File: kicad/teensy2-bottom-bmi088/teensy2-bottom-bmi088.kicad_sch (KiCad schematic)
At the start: 11 parts, among them J1 Conn_01x14_Socket, J2 Conn_01x14_Socket, J3 Conn_01x03_Socket, J4 Conn_01x03_Socket, J5 Conn_01x06_Pin, J6 Conn_01x02_Socket, J7 Conn_01x08_Pin

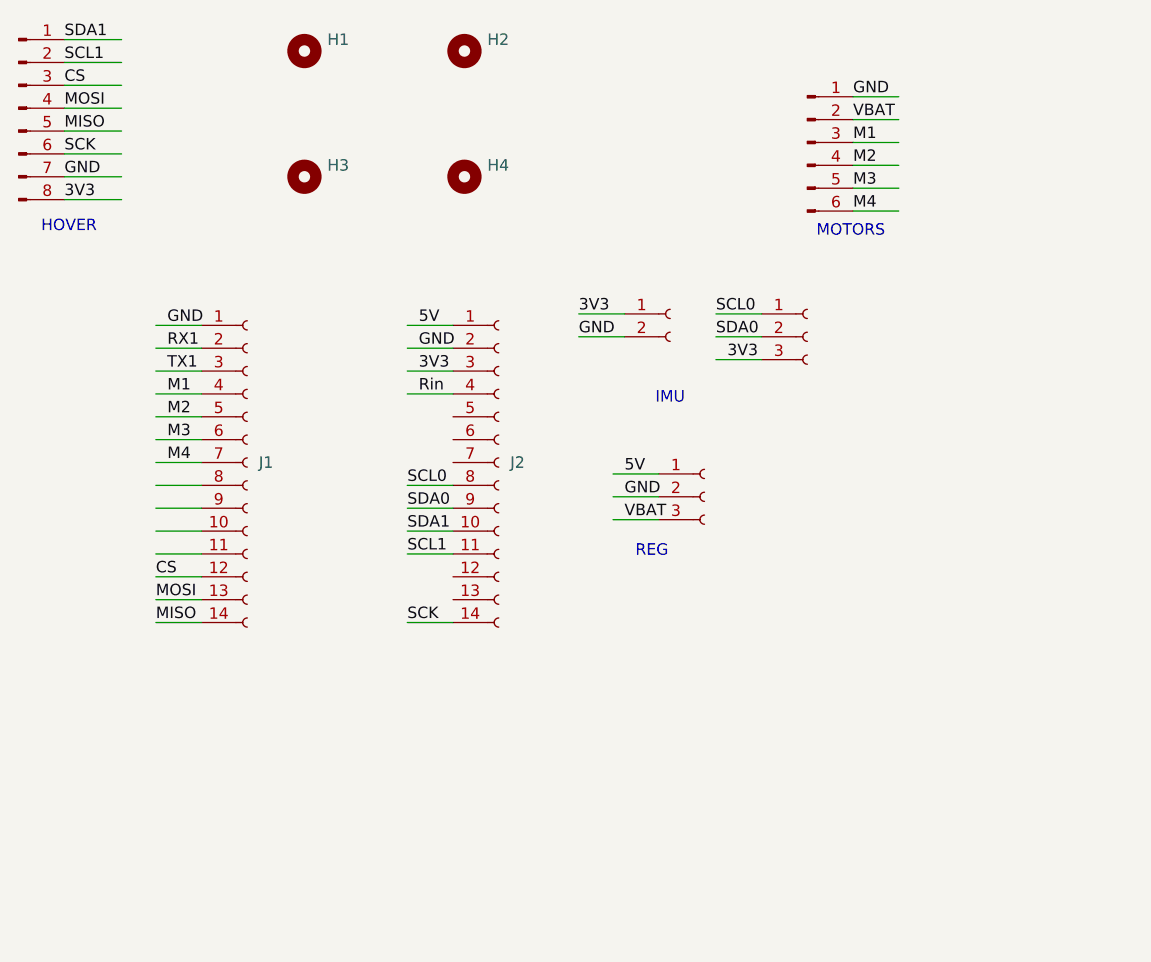
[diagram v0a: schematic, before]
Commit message: modified:   kicad/teensy2-bottom-bmi088/teensy2-bottom-bmi088.kicad_pcb
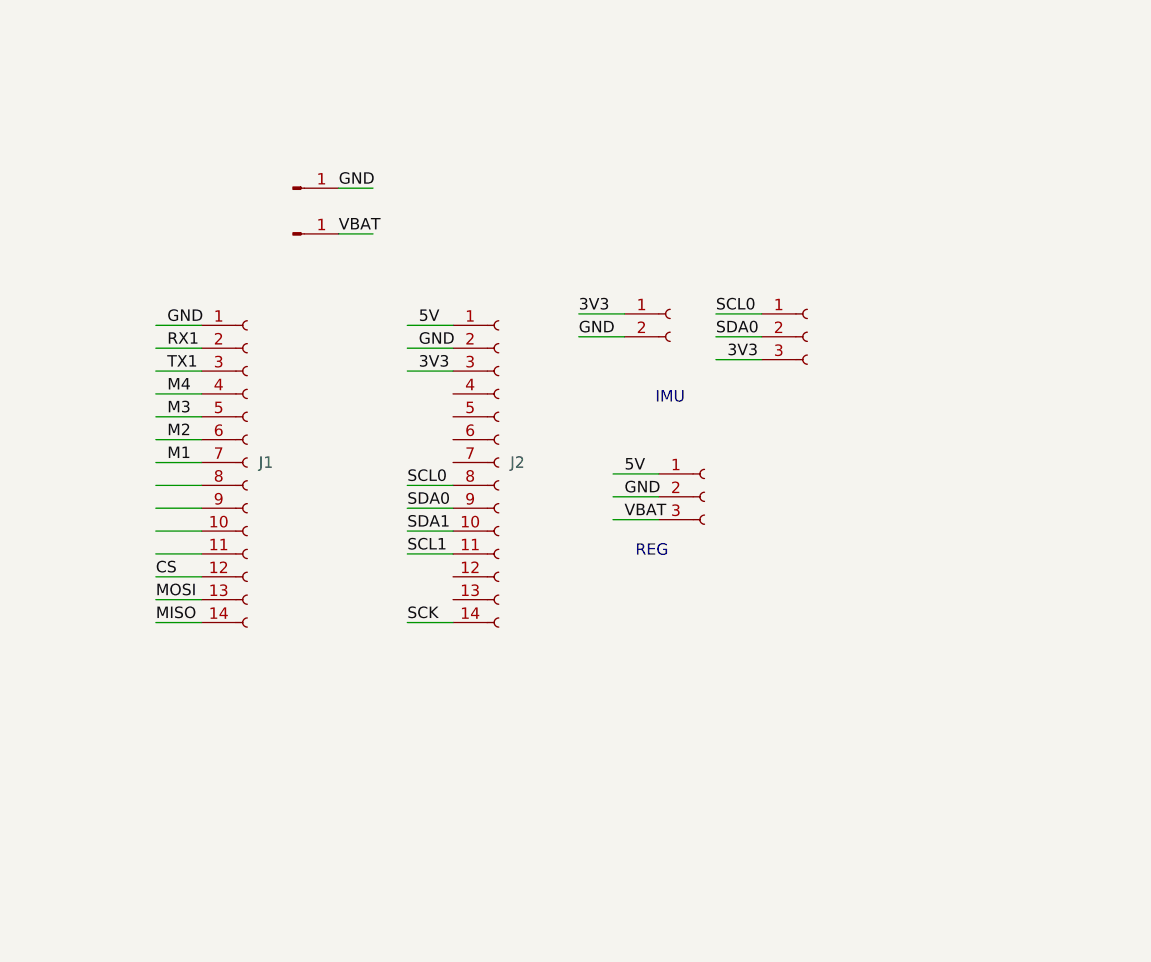
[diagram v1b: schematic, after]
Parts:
- removed H1, H2, H3, H4: MountingHole, MountingHole:MountingHole_2.5mm, symbol Mechanical:MountingHole
- removed J5: Conn_01x06_Pin, Connector_PinHeader_2.00mm:PinHeader_1x06_P2.00mm_Vertical, symbol Connector:Conn_01x06_Pin
- removed J7: Conn_01x08_Pin, Connector_PinSocket_2.00mm:PinSocket_1x08_P2.00mm_Vertical, symbol Connector:Conn_01x08_Pin
- added J5, J7: Conn_01x01_Pin, Connector_Wire:SolderWirePad_1x01_SMD_1x2mm, symbol Connector:Conn_01x01_Pin
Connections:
- net GND: now also J5.1 (Pin_1)
- net M1: now also J1.7 (Pin_7); no longer J1.4 (Pin_4)
- net M2: now also J1.6 (Pin_6); no longer J1.5 (Pin_5)
- net M3: now also J1.5 (Pin_5); no longer J1.6 (Pin_6)
- net M4: now also J1.4 (Pin_4); no longer J1.7 (Pin_7)
- net VBAT: now also J7.1 (Pin_1)
- net Rin: no longer names the net of J2.4 (Pin_4)
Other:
- note removed: "HOVER"
- note removed: "MOTORS"

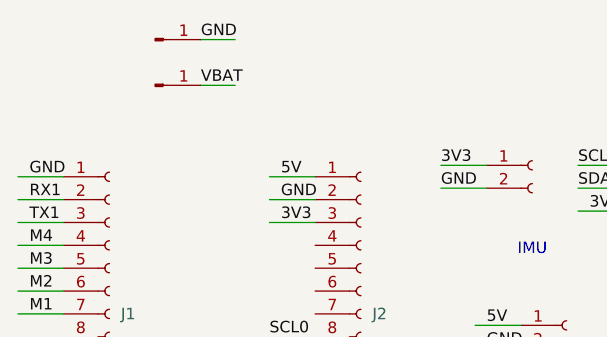
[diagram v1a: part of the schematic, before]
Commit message: modified:   kicad/teensy2-bottom-bmi088/teensy2-bottom-bmi088.kicad_pcb
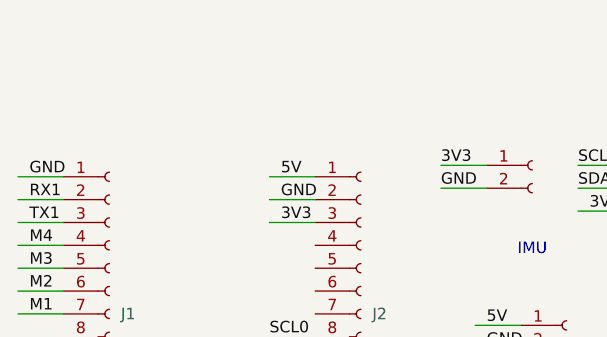
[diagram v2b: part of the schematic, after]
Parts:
- removed J5, J7: Conn_01x01_Pin, Connector_Wire:SolderWirePad_1x01_SMD_1x2mm, symbol Connector:Conn_01x01_Pin
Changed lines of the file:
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@@
-	(wire
-		(pts
-			(xy 111.76 88.9) (xy 115.57 88.9)
-		)
-		(stroke
-			(width 0)
-			(type default)
-		)
-	)
 	(wire
 		(pts
@@
 		(pts
 			(xy 142.24 115.57) (xy 147.32 115.57)
-		)
-		(stroke
-			(width 0)
-			(type default)
-		)
-	)
-	(wire
-		(pts
-			(xy 111.76 83.82) (xy 115.57 83.82)
 		)
 		(stroke
@@
 		)
 	)
-	(label "VBAT"
-		(at 111.76 88.9 0)
-		(effects
-			(font
-				(size 1.27 1.27)
-			)
-			(justify left bottom)
-		)
-	)
 	(label "GND"
 		(at 143.51 118.11 0)
@@
 	(label "TX1"
 		(at 92.71 104.14 0)
-		(effects
-			(font
-				(size 1.27 1.27)
-			)
-			(justify left bottom)
-		)
-	)
-	(label "GND"
-		(at 111.76 83.82 0)
 		(effects
 			(font
@@
 					(unit 1)
 				)
-			)
-		)
-	)
-	(symbol
-		(lib_id "Connector:Conn_01x01_Pin")
-		(at 106.68 83.82 0)
-		(unit 1)
-		(exclude_from_sim no)
-		(in_bom yes)
-		(on_board yes)
-		(dnp no)
-		(fields_autoplaced yes)
-		(property "Reference" "J5"
-			(at 107.315 78.74 0)
-			(effects
-				(font
-					(size 1.27 1.27)
-				)
-				(hide yes)
-			)
-		)
-		(property "Value" "Conn_01x01_Pin"
-			(at 107.315 81.28 0)
-			(effects
-				(font
-					(size 1.27 1.27)
-				)
-				(hide yes)
-			)
-		)
-		(property "Footprint" "Connector_Wire:SolderWirePad_1x01_SMD_1x2mm"
-			(at 106.68 83.82 0)
-			(effects
-				(font
-					(size 1.27 1.27)
-				)
-				(hide yes)
-			)
-		)
-		(property "Datasheet" "~"
-			(at 106.68 83.82 0)
-			(effects
-				(font
-					(size 1.27 1.27)
-				)
-				(hide yes)
-			)
-		)
-		(property "Description" "Generic connector, single row, 01x01, script generated"
-			(at 106.68 83.82 0)
-			(effects
-				(font
-					(size 1.27 1.27)
-				)
-				(hide yes)
-			)
-		)
-		(pin "1"
-		)
-		(instances
-			(project ""
-				(path "/2b1f0318-b347-4cb8-9bbf-78e69ec66761"
-					(reference "J5")
-					(unit 1)
-				)
-			)
-		)
-	)
-	(symbol
-		(lib_id "Connector:Conn_01x01_Pin")
-		(at 106.68 88.9 0)
-		(unit 1)
-		(exclude_from_sim no)
-		(in_bom yes)
-		(on_board yes)
-		(dnp no)
-		(fields_autoplaced yes)
-		(property "Reference" "J7"
-			(at 107.315 83.82 0)
-			(effects
-				(font
-					(size 1.27 1.27)
-				)
-				(hide yes)
-			)
-		)
-		(property "Value" "Conn_01x01_Pin"
-			(at 107.315 86.36 0)
-			(effects
-				(font
-					(size 1.27 1.27)
-				)
-				(hide yes)
-			)
-		)
-		(property "Footprint" "Connector_Wire:SolderWirePad_1x01_SMD_1x2mm"
-			(at 106.68 88.9 0)
-			(effects
-				(font
-					(size 1.27 1.27)
-				)
-				(hide yes)
-			)
-		)
-		(property "Datasheet" "~"
-			(at 106.68 88.9 0)
-			(effects
-				(font
-					(size 1.27 1.27)
-				)
-				(hide yes)
-			)
-		)
-		(property "Description" "Generic connector, single row, 01x01, script generated"
-			(at 106.68 88.9 0)
-			(effects
-				(font
-					(size 1.27 1.27)
-				)
-				(hide yes)
-			)
-		)
-		(pin "1"
-		)
-		(instances
-			(project "teensy2-bottom-bmi088"
-				(path "/2b1f0318-b347-4cb8-9bbf-78e69ec66761"
-					(reference "J7")
-					(unit 1)
-				)

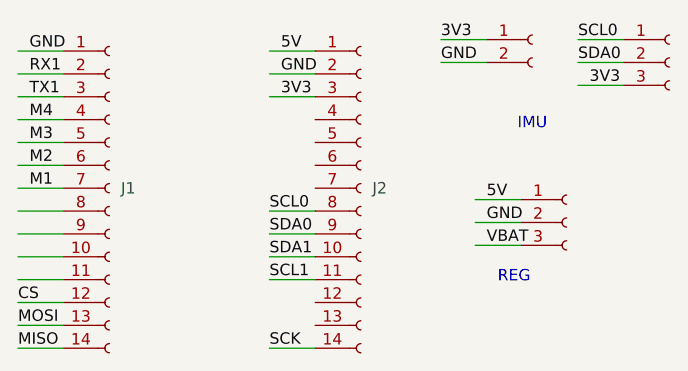
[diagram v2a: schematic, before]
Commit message: modified:   kicad/teensy2-bottom-bmi088/teensy2-bottom-bmi088.kicad_pcb
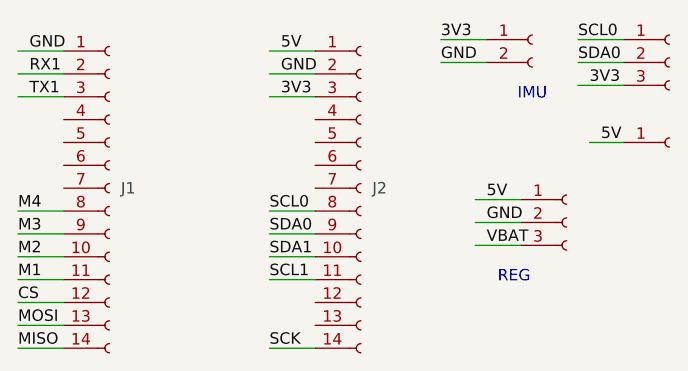
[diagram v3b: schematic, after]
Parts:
- added J5: Conn_01x01_Socket, Connector_Wire:SolderWirePad_1x01_SMD_1x2mm, symbol Connector:Conn_01x01_Socket
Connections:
- net 5V: now also J5.1 (Pin_1)
- net M1: now also J1.11 (Pin_11); no longer J1.7 (Pin_7)
- net M2: now also J1.10 (Pin_10); no longer J1.6 (Pin_6)
- net M3: now also J1.9 (Pin_9); no longer J1.5 (Pin_5)
- net M4: now also J1.8 (Pin_8); no longer J1.4 (Pin_4)
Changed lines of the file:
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@@
 	(text "IMU"
 		(exclude_from_sim no)
-		(at 148.59 107.188 0)
+		(at 148.59 103.886 0)
 		(effects
 			(font
@@
 	(wire
 		(pts
-			(xy 91.44 111.76) (xy 96.52 111.76)
-		)
-		(stroke
-			(width 0)
-			(type default)
-		)
-	)
-	(wire
-		(pts
 			(xy 91.44 101.6) (xy 96.52 101.6)
 		)
@@
 	(wire
 		(pts
-			(xy 91.44 106.68) (xy 96.52 106.68)
-		)
-		(stroke
-			(width 0)
-			(type default)
-		)
-	)
-	(wire
-		(pts
 			(xy 153.67 100.33) (xy 158.75 100.33)
 		)
@@
 	(wire
 		(pts
-			(xy 91.44 114.3) (xy 96.52 114.3)
-		)
-		(stroke
-			(width 0)
-			(type default)
-		)
-	)
-	(wire
-		(pts
 			(xy 91.44 116.84) (xy 96.52 116.84)
 		)
@@
 	(wire
 		(pts
-			(xy 91.44 109.22) (xy 96.52 109.22)
-		)
-		(stroke
-			(width 0)
-			(type default)
-		)
-	)
-	(wire
-		(pts
 			(xy 91.44 124.46) (xy 96.52 124.46)
 		)
@@
 		(pts
 			(xy 119.38 104.14) (xy 124.46 104.14)
+		)
+		(stroke
+			(width 0)
+			(type default)
+		)
+	)
+	(wire
+		(pts
+			(xy 154.94 109.22) (xy 158.75 109.22)
 		)
 		(stroke
@@
 		)
 	)
+	(label "M1"
+		(at 91.44 124.46 0)
+		(effects
+			(font
+				(size 1.27 1.27)
+			)
+			(justify left bottom)
+		)
+	)
 	(label "GND"
 		(at 92.71 99.06 0)
@@
 		)
 	)
+	(label "M2"
+		(at 91.44 121.92 0)
+		(effects
+			(font
+				(size 1.27 1.27)
+			)
+			(justify left bottom)
+		)
+	)
 	(label "MISO"
 		(at 91.44 132.08 0)
@@
 		)
 	)
+	(label "M4"
+		(at 91.44 116.84 0)
+		(effects
+			(font
+				(size 1.27 1.27)
+			)
+			(justify left bottom)
+		)
+	)
 	(label "SCL0"
 		(at 119.38 116.84 0)
@@
 		)
 	)
+	(label "M3"
+		(at 91.44 119.38 0)
+		(effects
+			(font
+				(size 1.27 1.27)
+			)
+			(justify left bottom)
+		)
+	)
 	(label "GND"
 		(at 143.51 118.11 0)
@@
 		)
 	)
-	(label "M1"
-		(at 92.71 114.3 0)
-		(effects
-			(font
-				(size 1.27 1.27)
-			)
-			(justify left bottom)
-		)
-	)
-	(label "M3"
-		(at 92.71 109.22 0)
-		(effects
-			(font
-				(size 1.27 1.27)
-			)
-			(justify left bottom)
-		)
-	)
-	(label "M2"
-		(at 92.71 111.76 0)
-		(effects
-			(font
-				(size 1.27 1.27)
-			)
-			(justify left bottom)
-		)
-	)
 	(label "3V3"
 		(at 138.43 97.79 0)
@@
 		)
 	)
-	(label "M4"
-		(at 92.71 106.68 0)
-		(effects
-			(font
-				(size 1.27 1.27)
-			)
-			(justify left bottom)
-		)
-	)
 	(label "TX1"
 		(at 92.71 104.14 0)
@@
 	(label "RX1"
 		(at 92.71 101.6 0)
+		(effects
+			(font
+				(size 1.27 1.27)
+			)
+			(justify left bottom)
+		)
+	)
+	(label "5V"
+		(at 156.21 109.22 0)
 		(effects
 			(font
@@
 					(unit 1)
 				)
+			)
+		)
+	)
+	(symbol
+		(lib_id "Connector:Conn_01x01_Socket")
+		(at 163.83 109.22 0)
+		(unit 1)
+		(exclude_from_sim no)
+		(in_bom yes)
+		(on_board yes)
+		(dnp no)
+		(fields_autoplaced yes)
+		(property "Reference" "J5"
+			(at 165.1 107.9499 0)
+			(effects
+				(font
+					(size 1.27 1.27)
+				)
+				(justify left)
+				(hide yes)
+			)
+		)
+		(property "Value" "Conn_01x01_Socket"
+			(at 165.1 110.4899 0)
+			(effects
+				(font
+					(size 1.27 1.27)
+				)
+				(justify left)
+				(hide yes)
+			)
+		)
+		(property "Footprint" "Connector_Wire:SolderWirePad_1x01_SMD_1x2mm"
+			(at 163.83 109.22 0)
+			(effects
+				(font
+					(size 1.27 1.27)
+				)
+				(hide yes)
+			)
+		)
+		(property "Datasheet" "~"
+			(at 163.83 109.22 0)
+			(effects
+				(font
+					(size 1.27 1.27)
+				)
+				(hide yes)
+			)
+		)
+		(property "Description" "Generic connector, single row, 01x01, script generated"
+			(at 163.83 109.22 0)
+			(effects
+				(font
+					(size 1.27 1.27)
+				)
+				(hide yes)
+			)
+		)
+		(pin "1"
+		)
+		(instances
+			(project ""
+				(path "/2b1f0318-b347-4cb8-9bbf-78e69ec66761"
+					(reference "J5")
+					(unit 1)
+				)

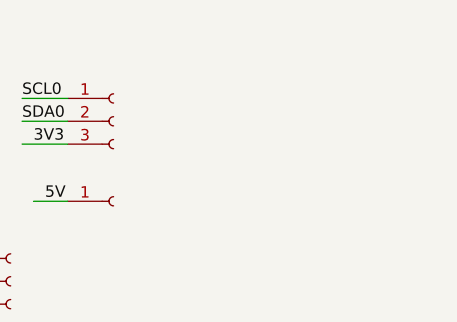
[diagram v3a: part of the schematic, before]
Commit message: modified:   kicad/teensy2-bottom-bmi088/teensy2-bottom-bmi088.kicad_pcb
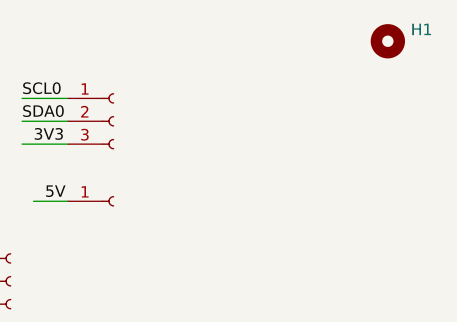
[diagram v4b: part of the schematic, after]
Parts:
- added H1: MountingHole, MountingHole:MountingHole_2.5mm, symbol Mechanical:MountingHole
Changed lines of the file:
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@@
+	)
+	(symbol
+		(lib_id "Mechanical:MountingHole")
+		(at 194.31 91.44 0)
+		(unit 1)
+		(exclude_from_sim no)
+		(in_bom no)
+		(on_board yes)
+		(dnp no)
+		(fields_autoplaced yes)
+		(property "Reference" "H1"
+			(at 196.85 90.1699 0)
+			(effects
+				(font
+					(size 1.27 1.27)
+				)
+				(justify left)
+			)
+		)
+		(property "Value" "MountingHole"
+			(at 196.85 92.7099 0)
+			(effects
+				(font
+					(size 1.27 1.27)
+				)
+				(justify left)
+				(hide yes)
+			)
+		)
+		(property "Footprint" "MountingHole:MountingHole_2.5mm"
+			(at 194.31 91.44 0)
+			(effects
+				(font
+					(size 1.27 1.27)
+				)
+				(hide yes)
+			)
+		)
+		(property "Datasheet" "~"
+			(at 194.31 91.44 0)
+			(effects
+				(font
+					(size 1.27 1.27)
+				)
+				(hide yes)
+			)
+		)
+		(property "Description" "Mounting Hole without connection"
+			(at 194.31 91.44 0)
+			(effects
+				(font
+					(size 1.27 1.27)
+				)
+				(hide yes)
+			)
+		)
+		(instances
+			(project "teensy2-bottom-bmi088"
+				(path "/2b1f0318-b347-4cb8-9bbf-78e69ec66761"
+					(reference "H1")
+					(unit 1)
+				)
+			)
+		)
 	)
 	(symbol

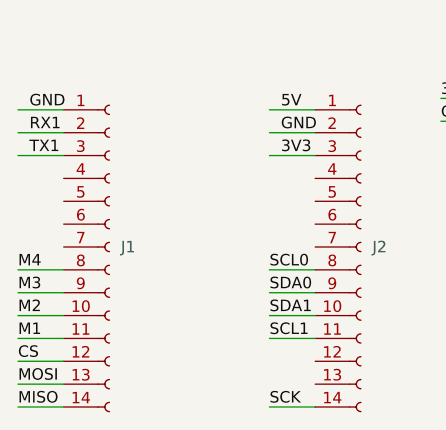
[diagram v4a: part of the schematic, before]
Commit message: modified:   kicad/teensy2-bottom-bmi088/teensy2-bottom-bmi088.kicad_pcb
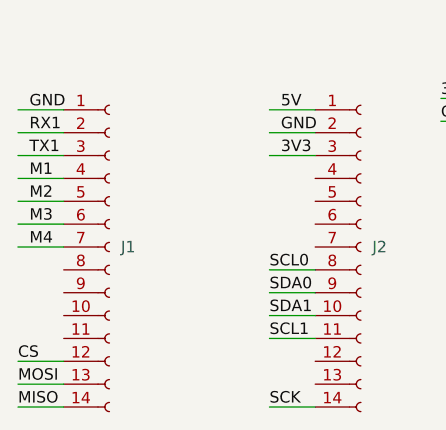
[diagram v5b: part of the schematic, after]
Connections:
- net M1: now also J1.4 (Pin_4); no longer J1.11 (Pin_11)
- net M2: now also J1.5 (Pin_5); no longer J1.10 (Pin_10)
- net M3: now also J1.6 (Pin_6); no longer J1.9 (Pin_9)
- net M4: now also J1.7 (Pin_7); no longer J1.8 (Pin_8)
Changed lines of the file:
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@@
+	(wire
+		(pts
+			(xy 91.44 114.3) (xy 96.52 114.3)
+		)
+		(stroke
+			(width 0)
+			(type default)
+		)
+	)
 	(wire
 		(pts
@@
 	(wire
 		(pts
+			(xy 91.44 111.76) (xy 96.52 111.76)
+		)
+		(stroke
+			(width 0)
+			(type default)
+		)
+	)
+	(wire
+		(pts
 			(xy 119.38 119.38) (xy 124.46 119.38)
 		)
@@
 	(wire
 		(pts
-			(xy 91.44 121.92) (xy 96.52 121.92)
-		)
-		(stroke
-			(width 0)
-			(type default)
-		)
-	)
-	(wire
-		(pts
 			(xy 153.67 100.33) (xy 158.75 100.33)
 		)
@@
 	(wire
 		(pts
-			(xy 91.44 116.84) (xy 96.52 116.84)
+			(xy 91.44 106.68) (xy 96.52 106.68)
 		)
 		(stroke
@@
 	(wire
 		(pts
+			(xy 91.44 109.22) (xy 96.52 109.22)
+		)
+		(stroke
+			(width 0)
+			(type default)
+		)
+	)
+	(wire
+		(pts
 			(xy 153.67 97.79) (xy 158.75 97.79)
 		)
@@
 		(pts
 			(xy 91.44 104.14) (xy 96.52 104.14)
-		)
-		(stroke
-			(width 0)
-			(type default)
-		)
-	)
-	(wire
-		(pts
-			(xy 91.44 124.46) (xy 96.52 124.46)
-		)
-		(stroke
-			(width 0)
-			(type default)
-		)
-	)
-	(wire
-		(pts
-			(xy 91.44 119.38) (xy 96.52 119.38)
 		)
 		(stroke
@@
 		)
 	)
-	(label "M1"
-		(at 91.44 124.46 0)
+	(label "M2"
+		(at 92.71 109.22 0)
 		(effects
 			(font
@@
 		)
 	)
-	(label "M2"
-		(at 91.44 121.92 0)
-		(effects
-			(font
-				(size 1.27 1.27)
-			)
-			(justify left bottom)
-		)
-	)
 	(label "MISO"
 		(at 91.44 132.08 0)
@@
 		)
 	)
-	(label "M4"
-		(at 91.44 116.84 0)
+	(label "M3"
+		(at 92.71 111.76 0)
 		(effects
 			(font
@@
 		)
 	)
-	(label "M3"
-		(at 91.44 119.38 0)
-		(effects
-			(font
-				(size 1.27 1.27)
-			)
-			(justify left bottom)
-		)
-	)
 	(label "GND"
 		(at 143.51 118.11 0)
@@
 		)
 	)
+	(label "M4"
+		(at 92.71 114.3 0)
+		(effects
+			(font
+				(size 1.27 1.27)
+			)
+			(justify left bottom)
+		)
+	)
 	(label "3V3"
 		(at 138.43 97.79 0)
@@
 		(effects
 			(font
+				(size 1.27 1.27)
+			)
+			(justify left bottom)
+		)
+	)
+	(label "M1"
+		(at 92.71 106.68 0)
+		(effects
+			(font
